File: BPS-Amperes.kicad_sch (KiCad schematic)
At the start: 55 parts, among them J1 ShuntConn, J2 LeaderConn, J3 Conn_01x04, U1 INA186A3IDDFT, U2 RO-123.3S_HP, U3 LTC6820, U4 HX1188FNL, U5 REF1930AIDDCT, U6 LTC2315, U7 OPA2196

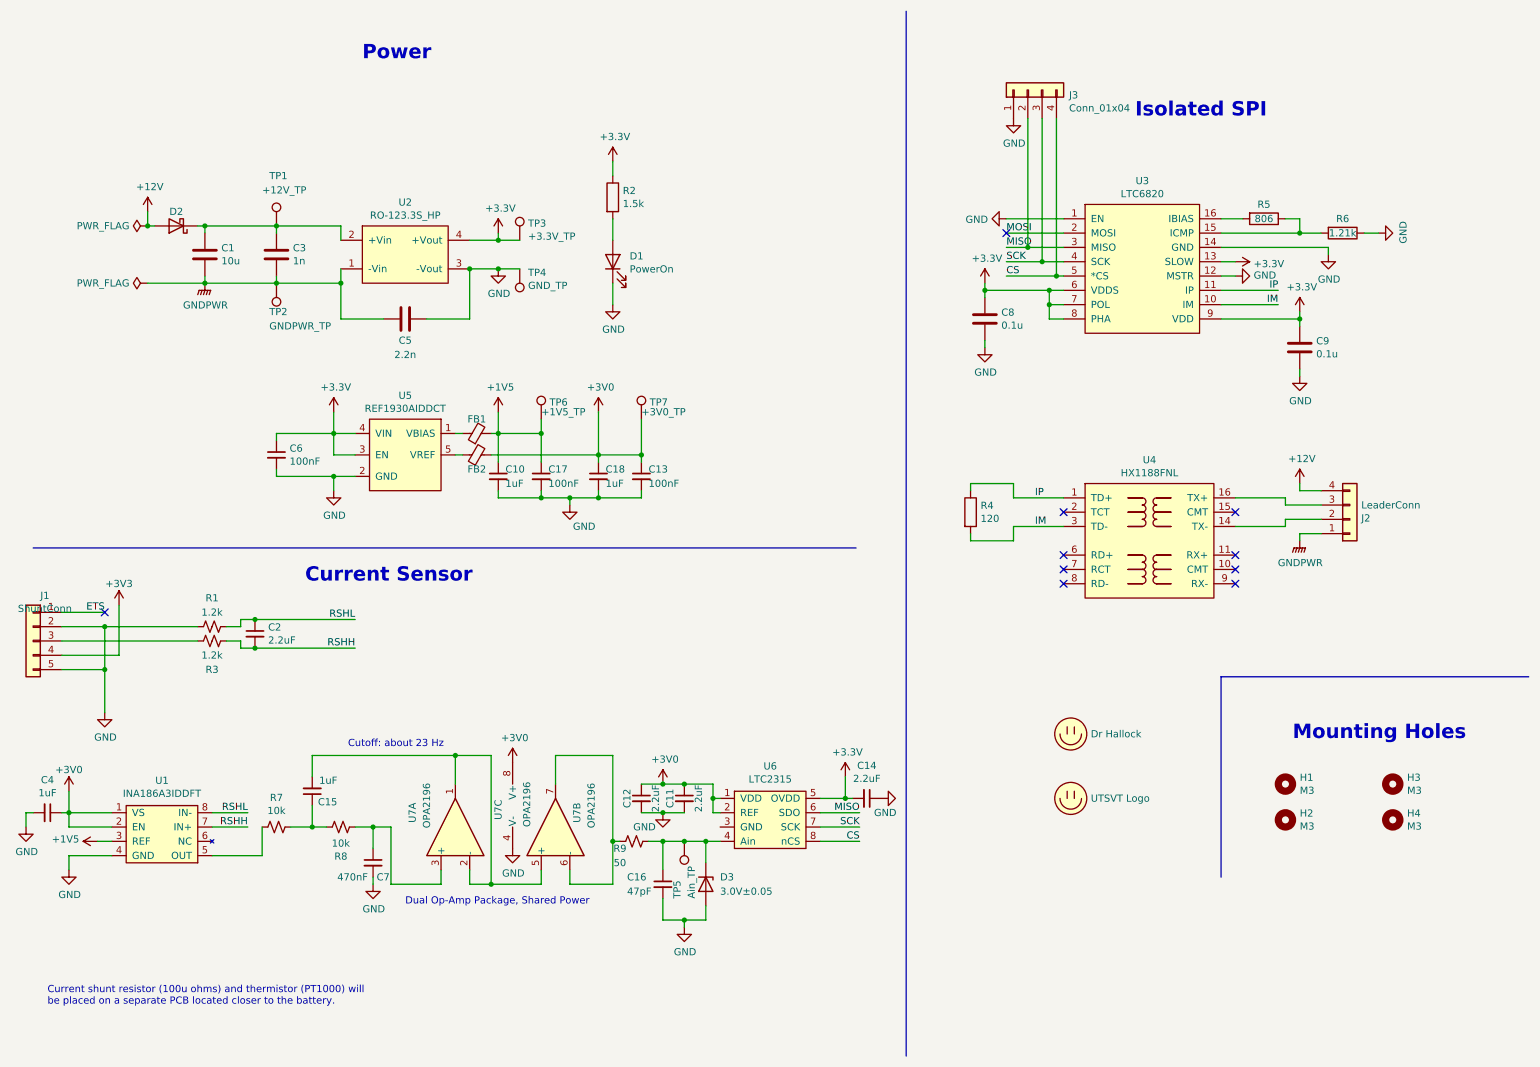
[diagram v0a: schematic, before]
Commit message: layout with no pours
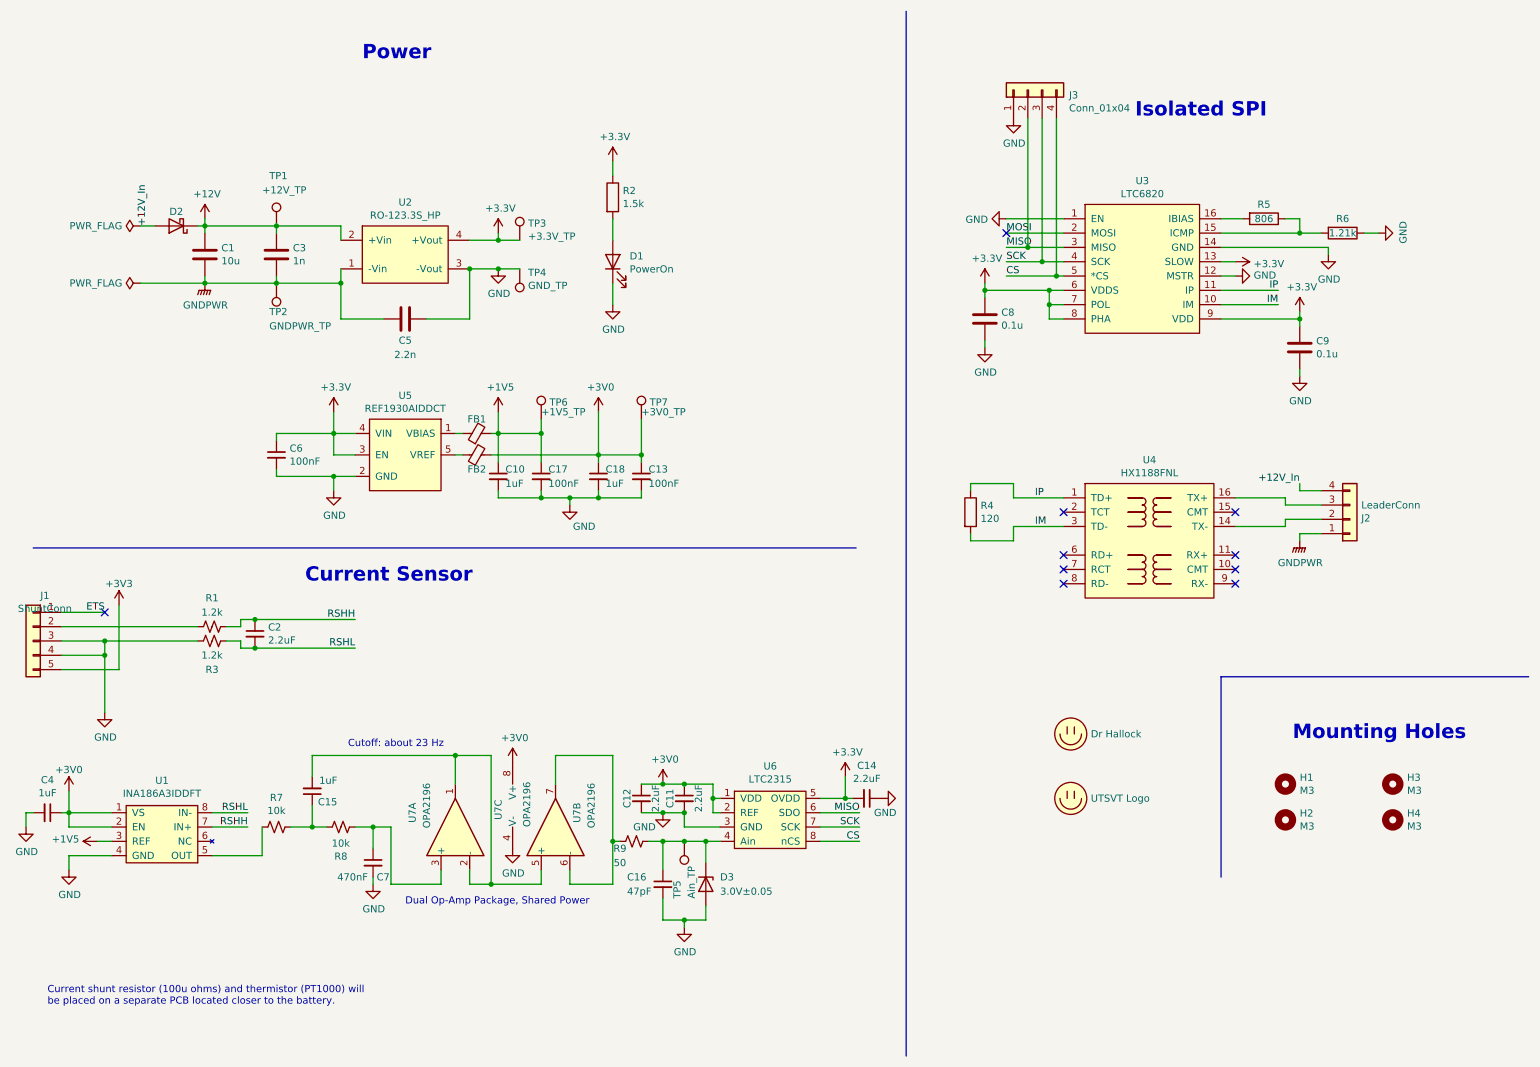
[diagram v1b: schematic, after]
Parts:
- J1: footprint Connector_PinSocket_2.54mm:PinSocket_1x05_P2.54mm_Horizontal -> Connector_PinSocket_2.54mm:PinSocket_1x05_P2.54mm_Vertical
- TP5: footprint (none) -> TestPoint:TestPoint_Keystone_5005-5009_Compact
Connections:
- net +12V: now also C1.1, C3.1, D2.1 (K), TP1.1, U2.2 (+Vin); no longer D2.2 (A), J2.4 (Pin_4)
- net +3V3: now also J1.5 (Pin_5); no longer J1.4 (Pin_4)
- net GND: now also J1.3 (Pin_3), J1.4 (Pin_4), R3.2, U6.3 (GND); no longer J1.2 (Pin_2), J1.5 (Pin_5), R1.2
- net RSHH: now also C2.1, R1.1; no longer C2.2, R3.1
- net RSHL: now also C2.2, R3.1; no longer C2.1, R1.1
- new net: J1.2 (Pin_2), R1.2
- new net +12V_In: D2.2 (A), J2.4 (Pin_4)

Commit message: add 👈 pass 💦 through 🐲 connector
and move 📦 things 🍄 around ➕🏜️➡️👤 a bit 😁
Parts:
- removed H1, H2, H3, H4: M3, MountingHole:MountingHole_3mm, symbol Mechanical:MountingHole
- added J4: Conn_01x05, Connector_PinHeader_2.54mm:PinHeader_1x05_P2.54mm_Vertical, symbol Connector_Generic:Conn_01x05
- TP1, TP2: footprint TestPoint:TestPoint_Keystone_5005-5009_Compact -> TestPoint:TestPoint_Pad_2.0x2.0mm
- TP3, TP4, TP6, TP7: footprint TestPoint:TestPoint_Keystone_5005-5009_Compact -> TestPoint:TestPoint_Pad_1.5x1.5mm
- TP5: footprint TestPoint:TestPoint_Keystone_5005-5009_Compact -> Connector_PinSocket_2.54mm:PinSocket_1x01_P2.54mm_Vertical
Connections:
- no-connect marks 10 -> 15
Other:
- note added: "Passthrough Connector (Physical Only)"
- note removed: "Mounting Holes"

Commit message: picket fence
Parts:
- J4: footprint Connector_PinHeader_2.54mm:PinHeader_1x05_P2.54mm_Vertical -> Connector_PinSocket_2.54mm:PinSocket_1x05_P2.54mm_Vertical
- TP5: footprint Connector_PinSocket_2.54mm:PinSocket_1x01_P2.54mm_Vertical -> Connector_PinHeader_2.54mm:PinHeader_1x01_P2.54mm_Vertical
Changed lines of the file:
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@@
       (effects (font (size 1.27 1.27)) (justify left))
     )
-    (property "Footprint" "Connector_PinHeader_2.54mm:PinHeader_1x05_P2.54mm_Vertical" (id 2) (at 254 144.78 0)
+    (property "Footprint" "Connector_PinSocket_2.54mm:PinSocket_1x05_P2.54mm_Vertical" (id 2) (at 254 144.78 0)
       (effects (font (size 1.27 1.27)) hide)
     )
@@
       (effects (font (size 1.27 1.27)) (justify right))
     )
-    (property "Footprint" "Connector_PinSocket_2.54mm:PinSocket_1x01_P2.54mm_Vertical" (id 2) (at 129.54 160.02 0)
+    (property "Footprint" "Connector_PinHeader_2.54mm:PinHeader_1x01_P2.54mm_Vertical" (id 2) (at 129.54 160.02 0)
       (effects (font (size 1.27 1.27)) hide)
     )
@@
     )
     (path "/6b53c5bb-48ec-4c1b-8864-b69a6ab98e1f"
-      (reference "J4") (unit 1) (value "Conn_01x05") (footprint "Connector_PinHeader_2.54mm:PinHeader_1x05_P2.54mm_Vertical")
+      (reference "J4") (unit 1) (value "Conn_01x05") (footprint "Connector_PinSocket_2.54mm:PinSocket_1x05_P2.54mm_Vertical")
     )
     (path "/00000000-0000-0000-0000-00005f35267c"
@@
     )
     (path "/b1a24d78-372b-4b1e-b7ee-2bdf1ef393bf"
-      (reference "TP5") (unit 1) (value "Ain_TP") (footprint "Connector_PinSocket_2.54mm:PinSocket_1x01_P2.54mm_Vertical")
+      (reference "TP5") (unit 1) (value "Ain_TP") (footprint "Connector_PinHeader_2.54mm:PinHeader_1x01_P2.54mm_Vertical")
     )
     (path "/59a495a6-d8de-43d4-8d89-de8bc9a5d6d1"

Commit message: fixed bom + ibom
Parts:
- C1: Mfg TMK212BBJ106MGHT -> C5750X7S2A106M230KB
- C10, C18: Mfg (none) -> C0805C105K5PACTU
- C13, C17, C6: Mfg (none) -> C0805C104M5RACTU
- D2: Mfg (none) -> NSVR0320MW2T1G; Mouser# RB061QS-20T18R -> (none)
- D3: Mfg BZT52H-A3V0-QX -> BZX38450-C3V0X
- FB1: Mfg (none) -> BK2125LM182-T
- J2: Mfg (none) -> 43650-0415
- J4: footprint Connector_PinSocket_2.54mm:PinSocket_1x05_P2.54mm_Vertical -> Connector_PinHeader_2.54mm:PinHeader_1x05_P2.54mm_Vertical
- TP5: footprint Connector_PinHeader_2.54mm:PinHeader_1x01_P2.54mm_Vertical -> Connector_PinSocket_2.54mm:PinSocket_1x01_P2.54mm_Vertical
- U1: Mfg (none) -> INA186A3IDDFT
- U5: Mfg (none) -> REF1930AIDDCT
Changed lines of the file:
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@@
+      (effects (font (size 1.27 1.27)) hide)
+    )
+    (property "Mfg" "43650-0415" (id 4) (at 252.73 102.87 0)
       (effects (font (size 1.27 1.27)) hide)
     )
@@
       (effects (font (size 1.27 1.27)) hide)
     )
-    (property "Mfg" "TMK212BBJ106MGHT" (id 4) (at 49.53 55.88 0)
+    (property "Mfg" "C5750X7S2A106M230KB" (id 4) (at 49.53 55.88 0)
       (effects (font (size 1.27 1.27)) hide)
     )
@@
     )
     (property "Datasheet" "" (id 3) (at 41.91 157.48 0)
+      (effects (font (size 1.27 1.27)) hide)
+    )
+    (property "Mfg" "INA186A3IDDFT " (id 4) (at 41.91 157.48 0)
       (effects (font (size 1.27 1.27)) hide)
     )
@@
       (effects (font (size 1.27 1.27)) hide)
     )
+    (property "Mfg" "REF1930AIDDCT" (id 4) (at 85.09 87.63 0)
+      (effects (font (size 1.27 1.27)) hide)
+    )
     (pin "1")
     (pin "2")
@@
       (effects (font (size 1.27 1.27)) hide)
     )
+    (property "Mfg" "C0805C104M5RACTU" (id 4) (at 62.23 91.44 0)
+      (effects (font (size 1.27 1.27)) hide)
+    )
     (pin "1")
     (pin "2")
@@
       (effects (font (size 1.27 1.27)) hide)
     )
+    (property "Mfg" "C0805C105K5PACTU" (id 4) (at 101.6 95.25 0)
+      (effects (font (size 1.27 1.27)) hide)
+    )
     (pin "1")
     (pin "2")
@@
     )
     (property "Datasheet" "https://www.mouser.com/ProductDetail/KEMET/C0805C104M5RACTU?qs=VOOUd%252Bza08qHu13WgNByHQ%3D%3D" (id 3) (at 127 95.25 0)
+      (effects (font (size 1.27 1.27)) hide)
+    )
+    (property "Mfg" "C0805C104M5RACTU" (id 4) (at 127 95.25 0)
       (effects (font (size 1.27 1.27)) hide)
     )
@@
       (effects (font (size 1.27 1.27)) hide)
     )
-    (property "Datasheet" "https://fscdn.rohm.com/en/products/databook/datasheet/discrete/diode/schottky_barrier/rb061qs-20-e.pdf" (id 3) (at 44.45 50.8 0)
-      (effects (font (size 1.27 1.27)) hide)
-    )
-    (property "Mouser#" "RB061QS-20T18R" (id 4) (at 44.45 50.8 0)
+    (property "Datasheet" "" (id 3) (at 44.45 50.8 0)
+      (effects (font (size 1.27 1.27)) hide)
+    )
+    (property "Mfg" "NSVR0320MW2T1G" (id 4) (at 44.45 50.8 0)
       (effects (font (size 1.27 1.27)) hide)
     )
@@
       (effects (font (size 1.27 1.27)) (justify left))
     )
-    (property "Footprint" "Connector_PinSocket_2.54mm:PinSocket_1x05_P2.54mm_Vertical" (id 2) (at 254 144.78 0)
+    (property "Footprint" "Connector_PinHeader_2.54mm:PinHeader_1x05_P2.54mm_Vertical" (id 2) (at 254 144.78 0)
       (effects (font (size 1.27 1.27)) hide)
     )
@@
       (effects (font (size 1.27 1.27)) hide)
     )
+    (property "Mfg" "C0805C104M5RACTU" (id 4) (at 109.22 95.25 0)
+      (effects (font (size 1.27 1.27)) hide)
+    )
     (pin "1")
     (pin "2")
@@
       (effects (font (size 1.27 1.27)) hide)
     )
+    (property "Mfg" "C0805C105K5PACTU" (id 4) (at 119.38 95.25 0)
+      (effects (font (size 1.27 1.27)) hide)
+    )
     (pin "1")
     (pin "2")
@@
       (effects (font (size 1.27 1.27)) hide)
     )
+    (property "Mfg" "BK2125LM182-T" (id 4) (at 97.79 87.63 90)
+      (effects (font (size 1.27 1.27)) hide)
+    )
     (pin "1")
     (pin "2")
@@
       (effects (font (size 1.27 1.27)) (justify right))
     )
-    (property "Footprint" "Connector_PinHeader_2.54mm:PinHeader_1x01_P2.54mm_Vertical" (id 2) (at 129.54 160.02 0)
+    (property "Footprint" "Connector_PinSocket_2.54mm:PinSocket_1x01_P2.54mm_Vertical" (id 2) (at 129.54 160.02 0)
       (effects (font (size 1.27 1.27)) hide)
     )
@@
       (effects (font (size 1.27 1.27)) hide)
     )
-    (property "Mfg" "BZT52H-A3V0-QX" (id 4) (at 138.43 167.64 90)
+    (property "Mfg" "BZX38450-C3V0X" (id 4) (at 138.43 167.64 90)
       (effects (font (size 1.27 1.27)) hide)
     )
@@
     )
     (path "/6b53c5bb-48ec-4c1b-8864-b69a6ab98e1f"
-      (reference "J4") (unit 1) (value "Conn_01x05") (footprint "Connector_PinSocket_2.54mm:PinSocket_1x05_P2.54mm_Vertical")
+      (reference "J4") (unit 1) (value "Conn_01x05") (footprint "Connector_PinHeader_2.54mm:PinHeader_1x05_P2.54mm_Vertical")
     )
     (path "/00000000-0000-0000-0000-00005f35267c"
@@
     )
     (path "/b1a24d78-372b-4b1e-b7ee-2bdf1ef393bf"
-      (reference "TP5") (unit 1) (value "Ain_TP") (footprint "Connector_PinHeader_2.54mm:PinHeader_1x01_P2.54mm_Vertical")
+      (reference "TP5") (unit 1) (value "Ain_TP") (footprint "Connector_PinSocket_2.54mm:PinSocket_1x01_P2.54mm_Vertical")
     )
     (path "/59a495a6-d8de-43d4-8d89-de8bc9a5d6d1"

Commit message: bom updates
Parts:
- C1: Mfg C5750X7S2A106M230KB -> CGA9N3X7S2A106K230KE
- FB1: Mfg BK2125LM182-T -> BLM21BD182SN1D
- FB2: Mfg (none) -> BLM21BD182SN1D
- R2: Mfg CRCW08051K50JNEB -> SDR10EZPJ152
- R5: Mfg CRCW0805806RFKEA -> CR0805-FX-8060ELF
- R9: Mfg CRCW080550R0FKTA -> MCU08050C4999FP500
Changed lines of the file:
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@@
       (effects (font (size 1.27 1.27)) hide)
     )
-    (property "Mfg" "CRCW0805806RFKEA" (id 4) (at 237.49 49.53 90)
+    (property "Mfg" "CR0805-FX-8060ELF" (id 4) (at 237.49 49.53 90)
       (effects (font (size 1.27 1.27)) hide)
     )
@@
       (effects (font (size 1.27 1.27)) hide)
     )
-    (property "Datasheet" "https://www.mouser.com/ProductDetail/810-C5750X7S2A106M " (id 3) (at 49.53 55.88 0)
-      (effects (font (size 1.27 1.27)) hide)
-    )
-    (property "Mfg" "C5750X7S2A106M230KB" (id 4) (at 49.53 55.88 0)
+    (property "Datasheet" "https://www.mouser.com/ProductDetail/TDK/CGA9N3X7S2A106K230KE?qs=FxQuwy19cyC8TXs2ZwvXNA%3D%3D" (id 3) (at 49.53 55.88 0)
+      (effects (font (size 1.27 1.27)) hide)
+    )
+    (property "Mfg" "CGA9N3X7S2A106K230KE" (id 4) (at 49.53 55.88 0)
       (effects (font (size 1.27 1.27)) hide)
     )
@@
       (effects (font (size 1.27 1.27)) hide)
     )
-    (property "Mfg" "CRCW08051K50JNEB" (id 4) (at 121.92 45.72 0)
+    (property "Mfg" "SDR10EZPJ152" (id 4) (at 121.92 45.72 0)
       (effects (font (size 1.27 1.27)) hide)
     )
@@
       (effects (font (size 1.27 1.27)) hide)
     )
-    (property "Mfg" "CRCW080550R0FKTA" (id 4) (at 125.73 160.02 90)
+    (property "Mfg" "MCU08050C4999FP500" (id 4) (at 125.73 160.02 90)
       (effects (font (size 1.27 1.27)) hide)
     )
@@
       (effects (font (size 1.27 1.27)) hide)
     )
-    (property "Datasheet" "https://www.mouser.com/ProductDetail/963-BK2125LM182-T" (id 3) (at 97.79 91.44 0)
+    (property "Datasheet" "https://www.mouser.com/ProductDetail/Murata-Electronics/BLM21BD182SN1D?qs=1w%252B2sDiFrrHE8EOZOaQSCA%3D%3D" (id 3) (at 97.79 91.44 0)
+      (effects (font (size 1.27 1.27)) hide)
+    )
+    (property "Mfg" "BLM21BD182SN1D" (id 4) (at 97.79 91.44 90)
       (effects (font (size 1.27 1.27)) hide)
     )
@@
       (effects (font (size 1.27 1.27)) hide)
     )
-    (property "Datasheet" "https://www.mouser.com/ProductDetail/963-BK2125LM182-T" (id 3) (at 97.79 87.63 0)
-      (effects (font (size 1.27 1.27)) hide)
-    )
-    (property "Mfg" "BK2125LM182-T" (id 4) (at 97.79 87.63 90)
-      (effects (font (size 1.27 1.27)) hide)
-    )
+    (property "Datasheet" "https://www.mouser.com/ProductDetail/Murata-Electronics/BLM21BD182SN1D?qs=1w%252B2sDiFrrHE8EOZOaQSCA%3D%3D" (id 3) (at 97.79 87.63 0)
+      (effects (font (size 1.27 1.27)) hide)
+    )
+    (property "Mfg" "BLM21BD182SN1D" (id 4) (at 97.79 87.63 90)
+      (effects (font (size 1.27 1.27)) hide)
+    )

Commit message: womp womp
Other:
- note removed: "Current Sensor"
- note removed: "Isolated SPI"
- note removed: "Power"
